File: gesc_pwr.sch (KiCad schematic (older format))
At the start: 48 parts, among them J10 PHASE_C, J11 PHASE_B, J12 NTC, J9 PHASE_A, Q1 BSC070N10NS5, Q2 BSC070N10NS5, Q3 BSC070N10NS5, Q4 BSC070N10NS5, Q5 BSC070N10NS5, Q6 BSC070N10NS5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

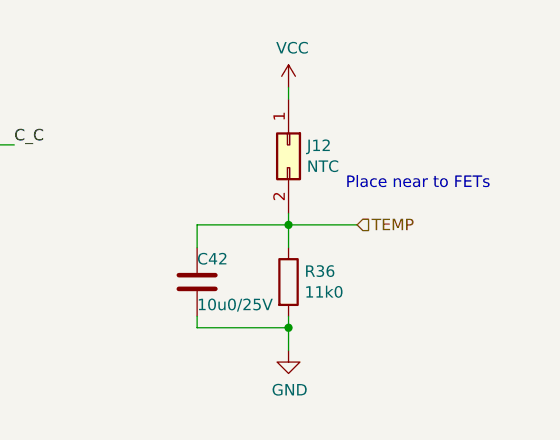
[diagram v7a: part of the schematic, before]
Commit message: - new driver 2ED2304S06F - separat Elkos for each phase - new FET placement
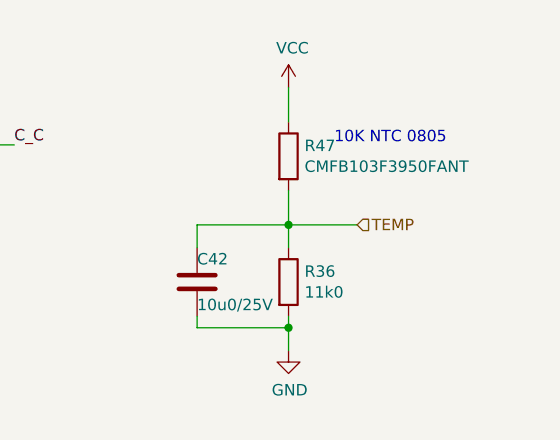
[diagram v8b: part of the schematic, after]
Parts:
- removed J12: NTC, gesc:2pad_smd_testpin, symbol Connector_Generic:Conn_02x01
- added R47: CMFB103F3950FANT, Resistor_SMD:R_0805_2012Metric, symbol Device:R
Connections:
- net TEMP: now also R47.2
- net VCC: now also R47.1
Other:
- note added: "10K NTC 0805"
- note removed: "Place near to FETs"
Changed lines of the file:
@@
 	1    0    0    -1
 $EndComp
-$Comp
-L Connector_Generic:Conn_02x01 J12
-U 1 1 5C01E678
-P 10050 1350
-F 0 "J12" V 10054 1430 50  0000 L CNN
-F 1 "NTC" V 10145 1430 50  0000 L CNN
-F 2 "gesc:2pad_smd_testpin" H 10050 1350 50  0001 C CNN
-F 3 "~" H 10050 1350 50  0001 C CNN
-	1    10050 1350
-	0    1    1    0
-$EndComp
-Wire Wire Line
-	10050 1150 10050 1100
-Wire Wire Line
-	10050 1650 10050 1700
 Wire Wire Line
 	9650 1800 9650 1700
@@
 	1    0    0    -1
 $EndComp
-Text Notes 10300 1550 0    50   ~ 0
-Place near to FETs
+Text Notes 10250 1350 0    50   ~ 0
+10K NTC 0805
 Wire Wire Line
 	10050 1700 10350 1700
@@
 	1    0    0    -1
 $EndComp
+$Comp
+L Device:R R47
+U 1 1 606B4BF8
+P 10050 1400
+F 0 "R47" H 10120 1446 50  0000 L CNN
+F 1 "CMFB103F3950FANT" H 10120 1355 50  0000 L CNN
+F 2 "Resistor_SMD:R_0805_2012Metric" V 9980 1400 50  0001 C CNN
+F 3 "~" H 10050 1400 50  0001 C CNN
+	1    10050 1400
+	1    0    0    -1
+$EndComp
+Wire Wire Line
+	10050 1550 10050 1700
+Wire Wire Line
+	10050 1100 10050 1250
 $EndSCHEMATC
